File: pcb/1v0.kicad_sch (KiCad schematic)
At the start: 10 parts, among them U2 TPSM82903

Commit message: changes to power tree
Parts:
- added 1V0: TestPoint, TestPoint:TestPoint_Pad_D1.0mm, symbol library:TestPoint
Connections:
- net 1V0_FD: now also 1V0.1
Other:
- moved on the sheet: C3, C4, C7, FB1, R15, R16, R17, R6, R7, U2

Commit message: moved stuff around, bom
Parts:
- removed C7: 0.1uF, Capacitor_SMD:C_0402_1005Metric, symbol library:C
- removed R15, R17: 100, Resistor_SMD:R_0402_1005Metric, symbol library:R_US
- added C4: 4.7nF, Capacitor_SMD:C_0402_1005Metric, symbol library:C
- added C6: 0.1uF, Capacitor_SMD:C_0402_1005Metric, symbol library:C
- added R10, R12: 100, Resistor_SMD:R_0402_1005Metric, symbol library:R_US
- C3: footprint (none) -> library:C_0402_1005Metric; Manufacturer (none) -> Murata Electronics; Manufacturer Product Number (none) -> GRM155R61A106ME11D
- C5: renamed from C4; footprint (none) -> library:C_0402_1005Metric; Manufacturer (none) -> Murata Electronics; Manufacturer Product Number (none) -> GRM155R71C224KA12D
- R11: renamed from R16; footprint Resistor_SMD:R_0603_1608Metric -> Resistor_SMD:R_1206_3216Metric; Manufacturer (none) -> Vishay Dale; Manufacturer Product Number (none) -> WSLP12065L000FEA
- R8: renamed from R6; value R_US -> 10K 1%; footprint (none) -> library:R_0402_1005Metric; Manufacturer (none) -> Vishay Dale; Manufacturer Product Number (none) -> CRCW040210K0FKED
- R9: renamed from R7; value R_US -> 15K 1%; footprint (none) -> library:R_0402_1005Metric; Manufacturer (none) -> Vishay Dale; Manufacturer Product Number (none) -> CRCW040215K0FKED
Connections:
- net 1V0_FD: now also R12.2
- net 1V0_P: now also R10.2
- net 1V0_SENS_N: now also C6.1, R10.1
- net 1V0_SENS_P: now also C6.2, R12.1
- net GND: now also C4.2
- net at U2.5 (SS/TR): now also C4.1
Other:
- moved on the sheet: C3

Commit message: decoupling
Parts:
- R10, R12: value 100 -> 10; Manufacturer Product Number RC0402FR-07100RL -> RC0402FR-0710RL
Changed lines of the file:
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@@
-	(symbol
-		(lib_id "library:R_US")
-		(at 180.34 87.63 180)
-		(unit 1)
-		(exclude_from_sim no)
-		(in_bom yes)
-		(on_board yes)
-		(dnp no)
-		(property "Reference" "R12"
-			(at 182.88 86.36 0)
-			(effects
-				(font
-					(size 1.27 1.27)
-				)
-				(justify right)
-			)
-		)
-		(property "Value" "100"
-			(at 182.88 88.9 0)
-			(effects
-				(font
-					(size 1.27 1.27)
-				)
-				(justify right)
-			)
-		)
-		(property "Footprint" "Resistor_SMD:R_0402_1005Metric"
-			(at 179.324 87.376 90)
-			(effects
-				(font
-					(size 1.27 1.27)
-				)
-				(hide yes)
-			)
-		)
-		(property "Datasheet" "~"
-			(at 180.34 87.63 0)
-			(effects
-				(font
-					(size 1.27 1.27)
-				)
-				(hide yes)
-			)
-		)
-		(property "Description" "RES 100 OHM 1% 1/16W 0402"
-			(at 180.34 87.63 0)
-			(effects
-				(font
-					(size 1.27 1.27)
-				)
-				(hide yes)
-			)
-		)
-		(property "Manufacturer" "YAGEO"
-			(at 180.34 87.63 0)
-			(effects
-				(font
-					(size 1.27 1.27)
-				)
-				(hide yes)
-			)
-		)
-		(property "Manufacturer Product Number" "RC0402FR-07100RL"
-			(at 180.34 87.63 0)
-			(effects
-				(font
-					(size 1.27 1.27)
-				)
-				(hide yes)
-			)
-		)
-		(pin "1"
-		)
-		(pin "2"
-		)
-		(instances
-			(project "RPi-HwAB-1"
-				(path "/e63e39d7-6ac0-4ffd-8aa3-1841a4541b55/f9ebb56c-78c7-42ac-bc19-ccbf788f5318/543b0287-b025-45f5-b3a0-69295c58de1f"
-					(reference "R12")
-					(unit 1)
-				)
-			)
-		)
-	)
 	(symbol
 		(lib_id "library:R_US")
@@
 	)
 	(symbol
-		(lib_id "library:R_US")
-		(at 167.64 87.63 180)
-		(unit 1)
-		(exclude_from_sim no)
-		(in_bom yes)
-		(on_board yes)
-		(dnp no)
-		(property "Reference" "R10"
-			(at 165.1 86.36 0)
-			(effects
-				(font
-					(size 1.27 1.27)
-				)
-				(justify left)
-			)
-		)
-		(property "Value" "100"
-			(at 165.1 88.9 0)
-			(effects
-				(font
-					(size 1.27 1.27)
-				)
-				(justify left)
-			)
-		)
-		(property "Footprint" "Resistor_SMD:R_0402_1005Metric"
-			(at 166.624 87.376 90)
-			(effects
-				(font
-					(size 1.27 1.27)
-				)
-				(hide yes)
-			)
-		)
-		(property "Datasheet" "~"
-			(at 167.64 87.63 0)
-			(effects
-				(font
-					(size 1.27 1.27)
-				)
-				(hide yes)
-			)
-		)
-		(property "Description" "RES 100 OHM 1% 1/16W 0402"
-			(at 167.64 87.63 0)
-			(effects
-				(font
-					(size 1.27 1.27)
-				)
-				(hide yes)
-			)
-		)
-		(property "Manufacturer" "YAGEO"
-			(at 167.64 87.63 0)
-			(effects
-				(font
-					(size 1.27 1.27)
-				)
-				(hide yes)
-			)
-		)
-		(property "Manufacturer Product Number" "RC0402FR-07100RL"
-			(at 167.64 87.63 0)
-			(effects
-				(font
-					(size 1.27 1.27)
-				)
-				(hide yes)
-			)
-		)
-		(pin "1"
-		)
-		(pin "2"
-		)
-		(instances
-			(project "RPi-HwAB-1"
-				(path "/e63e39d7-6ac0-4ffd-8aa3-1841a4541b55/f9ebb56c-78c7-42ac-bc19-ccbf788f5318/543b0287-b025-45f5-b3a0-69295c58de1f"
-					(reference "R10")
-					(unit 1)
-				)
-			)
-		)
-	)
-	(symbol
 		(lib_id "library:C")
 		(at 78.74 107.95 0)
@@
 	)
 	(symbol
+		(lib_id "library:R_US")
+		(at 167.64 87.63 180)
+		(unit 1)
+		(exclude_from_sim no)
+		(in_bom yes)
+		(on_board yes)
+		(dnp no)
+		(property "Reference" "R10"
+			(at 165.1 86.36 0)
+			(effects
+				(font
+					(size 1.27 1.27)
+				)
+				(justify left)
+			)
+		)
+		(property "Value" "10"
+			(at 165.1 88.9 0)
+			(effects
+				(font
+					(size 1.27 1.27)
+				)
+				(justify left)
+			)
+		)
+		(property "Footprint" "Resistor_SMD:R_0402_1005Metric"
+			(at 166.624 87.376 90)
+			(effects
+				(font
+					(size 1.27 1.27)
+				)
+				(hide yes)
+			)
+		)
+		(property "Datasheet" "~"
+			(at 167.64 87.63 0)
+			(effects
+				(font
+					(size 1.27 1.27)
+				)
+				(hide yes)
+			)
+		)
+		(property "Description" "RES 10 OHM 1% 1/16W 0402"
+			(at 167.64 87.63 0)
+			(effects
+				(font
+					(size 1.27 1.27)
+				)
+				(hide yes)
+			)
+		)
+		(property "Manufacturer" "YAGEO"
+			(at 167.64 87.63 0)
+			(effects
+				(font
+					(size 1.27 1.27)
+				)
+				(hide yes)
+			)
+		)
+		(property "Manufacturer Product Number" "RC0402FR-0710RL"
+			(at 167.64 87.63 0)
+			(effects
+				(font
+					(size 1.27 1.27)
+				)
+				(hide yes)
+			)
+		)
+		(property "Name" ""
+			(at 167.64 87.63 0)
+			(effects
+				(font
+					(size 1.27 1.27)
+				)
+				(hide yes)
+			)
+		)
+		(pin "1"
+		)
+		(pin "2"
+		)
+		(instances
+			(project "RPi-HwAB-1"
+				(path "/e63e39d7-6ac0-4ffd-8aa3-1841a4541b55/f9ebb56c-78c7-42ac-bc19-ccbf788f5318/543b0287-b025-45f5-b3a0-69295c58de1f"
+					(reference "R10")
+					(unit 1)
+				)
+			)
+		)
+	)
+	(symbol
 		(lib_id "library:GND")
 		(at 78.74 114.3 0)
@@
 					(unit 1)
 				)
+			)
+		)
+	)
+	(symbol
+		(lib_id "library:R_US")
+		(at 180.34 87.63 180)
+		(unit 1)
+		(exclude_from_sim no)
+		(in_bom yes)
+		(on_board yes)
+		(dnp no)
+		(property "Reference" "R12"
+			(at 182.88 86.36 0)
+			(effects
+				(font
+					(size 1.27 1.27)
+				)
+				(justify right)
+			)
+		)
+		(property "Value" "10"
+			(at 182.88 88.9 0)
+			(effects
+				(font
+					(size 1.27 1.27)
+				)
+				(justify right)
+			)
+		)
+		(property "Footprint" "Resistor_SMD:R_0402_1005Metric"
+			(at 179.324 87.376 90)
+			(effects
+				(font
+					(size 1.27 1.27)
+				)
+				(hide yes)
+			)
+		)
+		(property "Datasheet" "~"
+			(at 180.34 87.63 0)
+			(effects
+				(font
+					(size 1.27 1.27)
+				)
+				(hide yes)
+			)
+		)
+		(property "Description" "RES 10 OHM 1% 1/16W 0402"
+			(at 180.34 87.63 0)
+			(effects
+				(font
+					(size 1.27 1.27)
+				)
+				(hide yes)
+			)
+		)
+		(property "Manufacturer" "YAGEO"
+			(at 180.34 87.63 0)
+			(effects
+				(font
+					(size 1.27 1.27)
+				)
+				(hide yes)
+			)
+		)
+		(property "Manufacturer Product Number" "RC0402FR-0710RL"
+			(at 180.34 87.63 0)
+			(effects
+				(font
+					(size 1.27 1.27)
+				)
+				(hide yes)
+			)
+		)
+		(property "Name" ""
+			(at 180.34 87.63 0)
+			(effects
+				(font
+					(size 1.27 1.27)
+				)
+				(hide yes)
+			)
+		)
+		(pin "1"
+		)
+		(pin "2"
+		)
+		(instances
+			(project "RPi-HwAB-1"
+				(path "/e63e39d7-6ac0-4ffd-8aa3-1841a4541b55/f9ebb56c-78c7-42ac-bc19-ccbf788f5318/543b0287-b025-45f5-b3a0-69295c58de1f"
+					(reference "R12")
+					(unit 1)
+				)

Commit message: bom
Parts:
- 1V0: now left out of the parts list
- C3: footprint library:C_0402_1005Metric -> Capacitor_SMD:C_0402_1005Metric; Part Description (none) -> CAP CER 10UF 10V X5R 0402
- C4: Part Description (none) -> CAP CER 0402 4.7NF 50V X7R 5%
- C5: footprint library:C_0402_1005Metric -> Capacitor_SMD:C_0603_1608Metric; Manufacturer Product Number GRM155R71C224KA12D -> GRM188R61A226ME15D; Part Description (none) -> CAP CER 22UF 10V X5R 0603
- C6: Part Description (none) -> CAP CER 0.1UF 16V X7R 0402
- FB1: value FerriteBead -> 120R @ 100MHz; footprint (none) -> Inductor_SMD:L_0603_1608Metric; Manufacturer (none) -> Murata Electronics; Manufacturer Product Number (none) -> BLM18KG121TN1D; Part Description (none) -> FERRITE BEAD 120 OHM 0603 1LN
- R10: renamed from R9; footprint library:R_0402_1005Metric -> Resistor_SMD:R_0402_1005Metric; Part Description (none) -> RES 15K OHM 1% 1/16W 0402
- R11: renamed from R10; Part Description (none) -> RES 10 OHM 1% 1/16W 0402
- R12: renamed from R11; Part Description (none) -> RES 0.005 OHM 1% 1W 1206
- R13: renamed from R12; Part Description (none) -> RES 10 OHM 1% 1/16W 0402
- R9: renamed from R8; footprint library:R_0402_1005Metric -> Resistor_SMD:R_0402_1005Metric; Part Description (none) -> RES 10K OHM 1% 1/16W 0402
- U2: Part Description (none) -> 3-V TO 17-V, 3-A, HIGH-EFFICIENC
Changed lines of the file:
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@@
 		(on_board yes)
 		(dnp no)
-		(property "Reference" "R11"
+		(property "Reference" "R12"
 			(at 173.99 77.47 90)
 			(effects
@@
 			)
 		)
+		(property "Part Description" "RES 0.005 OHM 1% 1W 1206"
+			(at 173.99 81.28 90)
+			(effects
+				(font
+					(size 1.27 1.27)
+				)
+				(hide yes)
+			)
+		)
 		(pin "1"
 		)
@@
 			(project "RPi-HwAB-1"
 				(path "/e63e39d7-6ac0-4ffd-8aa3-1841a4541b55/f9ebb56c-78c7-42ac-bc19-ccbf788f5318/543b0287-b025-45f5-b3a0-69295c58de1f"
-					(reference "R11")
+					(reference "R12")
 					(unit 1)
 				)
@@
 			)
 		)
-		(property "Datasheet" ""
+		(property "Datasheet" "~"
 			(at 78.74 107.95 0)
 			(effects
@@
 		)
 		(property "Name" ""
+			(at 78.74 107.95 0)
+			(effects
+				(font
+					(size 1.27 1.27)
+				)
+				(hide yes)
+			)
+		)
+		(property "Part Description" "CAP CER 0402 4.7NF 50V X7R 5%"
 			(at 78.74 107.95 0)
 			(effects
@@
 			)
 		)
-		(property "Value" "FerriteBead"
+		(property "Value" "120R @ 100MHz"
 			(at 210.7692 86.36 90)
 			(effects
@@
 			)
 		)
-		(property "Footprint" ""
+		(property "Footprint" "Inductor_SMD:L_0603_1608Metric"
 			(at 210.82 93.218 90)
 			(effects
@@
 		(property "Description" "Ferrite bead"
 			(at 210.82 91.44 0)
+			(effects
+				(font
+					(size 1.27 1.27)
+				)
+				(hide yes)
+			)
+		)
+		(property "Manufacturer" "Murata Electronics"
+			(at 210.82 91.44 90)
+			(effects
+				(font
+					(size 1.27 1.27)
+				)
+				(hide yes)
+			)
+		)
+		(property "Manufacturer Product Number" "BLM18KG121TN1D"
+			(at 210.82 91.44 90)
+			(effects
+				(font
+					(size 1.27 1.27)
+				)
+				(hide yes)
+			)
+		)
+		(property "Name" ""
+			(at 210.82 91.44 0)
+			(effects
+				(font
+					(size 1.27 1.27)
+				)
+				(hide yes)
+			)
+		)
+		(property "Part Description" "FERRITE BEAD 120 OHM 0603 1LN"
+			(at 210.82 91.44 90)
 			(effects
 				(font
@@
 			)
 		)
+		(property "Part Description" "3-V TO 17-V, 3-A, HIGH-EFFICIENC"
+			(at 106.68 96.52 0)
+			(effects
+				(font
+					(size 1.27 1.27)
+				)
+				(hide yes)
+			)
+		)
 		(pin "11"
 		)
@@
 		(on_board yes)
 		(dnp no)
-		(property "Reference" "R10"
+		(property "Reference" "R11"
 			(at 165.1 86.36 0)
 			(effects
@@
 			)
 		)
+		(property "Part Description" "RES 10 OHM 1% 1/16W 0402"
+			(at 167.64 87.63 0)
+			(effects
+				(font
+					(size 1.27 1.27)
+				)
+				(hide yes)
+			)
+		)
 		(pin "1"
 		)
@@
 			(project "RPi-HwAB-1"
 				(path "/e63e39d7-6ac0-4ffd-8aa3-1841a4541b55/f9ebb56c-78c7-42ac-bc19-ccbf788f5318/543b0287-b025-45f5-b3a0-69295c58de1f"
-					(reference "R10")
+					(reference "R11")
 					(unit 1)
 				)
@@
 		(unit 1)
 		(exclude_from_sim no)
-		(in_bom yes)
+		(in_bom no)
 		(on_board yes)
 		(dnp no)
@@
 			)
 		)
+		(property "Name" ""
+			(at 231.14 66.04 0)
+			(effects
+				(font
+					(size 1.27 1.27)
+				)
+				(hide yes)
+			)
+		)
 		(pin "1"
 		)
@@
 		(dnp no)
 		(fields_autoplaced yes)
-		(property "Reference" "R9"
+		(property "Reference" "R10"
 			(at 137.16 99.0599 0)
 			(effects
@@
 			)
 		)
-		(property "Footprint" "library:R_0402_1005Metric"
+		(property "Footprint" "Resistor_SMD:R_0402_1005Metric"
 			(at 135.636 100.584 90)
 			(effects
@@
 			)
 		)
+		(property "Part Description" "RES 15K OHM 1% 1/16W 0402"
+			(at 134.62 100.33 0)
+			(effects
+				(font
+					(size 1.27 1.27)
+				)
+				(hide yes)
+			)
+		)
 		(pin "1"
 		)
@@
 			(project "RPi-HwAB-1"
 				(path "/e63e39d7-6ac0-4ffd-8aa3-1841a4541b55/f9ebb56c-78c7-42ac-bc19-ccbf788f5318/543b0287-b025-45f5-b3a0-69295c58de1f"
-					(reference "R9")
+					(reference "R10")
 					(unit 1)
 				)
@@
 		(on_board yes)
 		(dnp no)
-		(property "Reference" "R12"
+		(property "Reference" "R13"
 			(at 182.88 86.36 0)
 			(effects
@@
 			)
 		)
+		(property "Part Description" "RES 10 OHM 1% 1/16W 0402"
+			(at 180.34 87.63 0)
+			(effects
+				(font
+					(size 1.27 1.27)
+				)
+				(hide yes)
+			)
+		)
 		(pin "1"
 		)
@@
 			(project "RPi-HwAB-1"
 				(path "/e63e39d7-6ac0-4ffd-8aa3-1841a4541b55/f9ebb56c-78c7-42ac-bc19-ccbf788f5318/543b0287-b025-45f5-b3a0-69295c58de1f"
-					(reference "R12")
+					(reference "R13")
 					(unit 1)
 				)
@@
 		(dnp no)
 		(fields_autoplaced yes)
-		(property "Reference" "R8"
+		(property "Reference" "R9"
 			(at 137.16 86.3599 0)
 			(effects
@@
 			)
 		)
-		(property "Footprint" "library:R_0402_1005Metric"
+		(property "Footprint" "Resistor_SMD:R_0402_1005Metric"
 			(at 135.636 87.884 90)
 			(effects
@@
 			)
 		)
+		(property "Part Description" "RES 10K OHM 1% 1/16W 0402"
+			(at 134.62 87.63 0)
+			(effects
+				(font
+					(size 1.27 1.27)
+				)
+				(hide yes)
+			)
+		)
 		(pin "1"
 		)
@@
 			(project "RPi-HwAB-1"
 				(path "/e63e39d7-6ac0-4ffd-8aa3-1841a4541b55/f9ebb56c-78c7-42ac-bc19-ccbf788f5318/543b0287-b025-45f5-b3a0-69295c58de1f"
-					(reference "R8")
+					(reference "R9")
 					(unit 1)
 				)
@@
 			)
 		)
-		(property "Footprint" "library:C_0402_1005Metric"
+		(property "Footprint" "Capacitor_SMD:C_0402_1005Metric"
 			(at 72.0852 111.76 0)
 			(effects
@@
 		)
 		(property "Manufacturer Product Number" "GRM155R61A106ME11D"
+			(at 71.12 107.95 0)
+			(effects
+				(font
+					(size 1.27 1.27)
+				)
+				(hide yes)
+			)
+		)
+		(property "Part Description" "CAP CER 10UF 10V X5R 0402"
 			(at 71.12 107.95 0)
 			(effects
@@
 			)
 		)
+		(property "Part Description" "CAP CER 0.1UF 16V X7R 0402"
+			(at 173.99 96.52 90)
+			(effects
+				(font
+					(size 1.27 1.27)
+				)
+				(hide yes)
+			)
+		)
 		(pin "1"
 		)
@@
 			)
 		)
-		(property "Footprint" "library:C_0402_1005Metric"
+		(property "Footprint" "Capacitor_SMD:C_0603_1608Metric"
 			(at 146.3548 97.79 0)
 			(effects
@@
 			)
 		)
-		(property "Manufacturer Product Number" "GRM155R71C224KA12D"
+		(property "Manufacturer Product Number" "GRM188R61A226ME15D"
 			(at 147.32 93.98 0)
 			(effects
+				(font
+					(size 1.27 1.27)
+				)
+				(hide yes)
+			)
+		)
+		(property "Part Description" "CAP CER 22UF 10V X5R 0603"
+			(at 147.32 93.98 0)
+			(effects

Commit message: added mig ddr pinout constraints
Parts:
- C5: renamed from C3; footprint Capacitor_SMD:C_0402_1005Metric -> Capacitor_SMD:C_1206_3216Metric; Manufacturer Murata Electronics -> KYOCERA AVX; Manufacturer Product Number GRM155R61A106ME11D -> TAJA106M010RNJ; Part Description CAP CER 10UF 10V X5R 0402 -> CAP TANT 10UF 20% 10V 1206
- renumbered C5 to C3, C6 to C4, C4 to C6, R9 to R10, R13 to R12, R10 to R13, R12 to R9
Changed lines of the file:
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@@
 		(on_board yes)
 		(dnp no)
-		(property "Reference" "R12"
+		(property "Reference" "R9"
 			(at 173.99 77.47 90)
 			(effects
@@
 			(project "RPi-HwAB-1"
 				(path "/e63e39d7-6ac0-4ffd-8aa3-1841a4541b55/f9ebb56c-78c7-42ac-bc19-ccbf788f5318/543b0287-b025-45f5-b3a0-69295c58de1f"
-					(reference "R12")
+					(reference "R9")
 					(unit 1)
 				)
@@
 		(on_board yes)
 		(dnp no)
-		(property "Reference" "C4"
+		(property "Reference" "C6"
 			(at 82.55 106.68 0)
 			(effects
@@
 			(project "RPi-HwAB-1"
 				(path "/e63e39d7-6ac0-4ffd-8aa3-1841a4541b55/f9ebb56c-78c7-42ac-bc19-ccbf788f5318/543b0287-b025-45f5-b3a0-69295c58de1f"
-					(reference "C4")
+					(reference "C6")
 					(unit 1)
 				)
@@
 		(dnp no)
 		(fields_autoplaced yes)
-		(property "Reference" "R10"
+		(property "Reference" "R13"
 			(at 137.16 99.0599 0)
 			(effects
@@
 			(project "RPi-HwAB-1"
 				(path "/e63e39d7-6ac0-4ffd-8aa3-1841a4541b55/f9ebb56c-78c7-42ac-bc19-ccbf788f5318/543b0287-b025-45f5-b3a0-69295c58de1f"
-					(reference "R10")
+					(reference "R13")
 					(unit 1)
 				)
@@
 		(on_board yes)
 		(dnp no)
-		(property "Reference" "R13"
+		(property "Reference" "R12"
 			(at 182.88 86.36 0)
 			(effects
@@
 			(project "RPi-HwAB-1"
 				(path "/e63e39d7-6ac0-4ffd-8aa3-1841a4541b55/f9ebb56c-78c7-42ac-bc19-ccbf788f5318/543b0287-b025-45f5-b3a0-69295c58de1f"
-					(reference "R13")
+					(reference "R12")
 					(unit 1)
 				)
@@
 		(dnp no)
 		(fields_autoplaced yes)
-		(property "Reference" "R9"
+		(property "Reference" "R10"
 			(at 137.16 86.3599 0)
 			(effects
@@
 			(project "RPi-HwAB-1"
 				(path "/e63e39d7-6ac0-4ffd-8aa3-1841a4541b55/f9ebb56c-78c7-42ac-bc19-ccbf788f5318/543b0287-b025-45f5-b3a0-69295c58de1f"
-					(reference "R9")
+					(reference "R10")
 					(unit 1)
 				)
@@
 		(on_board yes)
 		(dnp no)
-		(property "Reference" "C3"
+		(property "Reference" "C5"
 			(at 67.31 106.6799 0)
 			(effects
@@
 			)
 		)
-		(property "Footprint" "Capacitor_SMD:C_0402_1005Metric"
+		(property "Footprint" "Capacitor_SMD:C_1206_3216Metric"
 			(at 72.0852 111.76 0)
 			(effects
@@
 			)
 		)
-		(property "Manufacturer" "Murata Electronics"
+		(property "Manufacturer" "KYOCERA AVX"
 			(at 71.12 107.95 0)
 			(effects
@@
 			)
 		)
-		(property "Manufacturer Product Number" "GRM155R61A106ME11D"
+		(property "Manufacturer Product Number" "TAJA106M010RNJ"
 			(at 71.12 107.95 0)
 			(effects
@@
 			)
 		)
-		(property "Part Description" "CAP CER 10UF 10V X5R 0402"
+		(property "Part Description" "CAP TANT 10UF 20% 10V 1206"
 			(at 71.12 107.95 0)
 			(effects
@@
 			(project "RPi-HwAB-1"
 				(path "/e63e39d7-6ac0-4ffd-8aa3-1841a4541b55/f9ebb56c-78c7-42ac-bc19-ccbf788f5318/543b0287-b025-45f5-b3a0-69295c58de1f"
-					(reference "C3")
+					(reference "C5")
 					(unit 1)
 				)
@@
 		(dnp no)
 		(fields_autoplaced yes)
-		(property "Reference" "C6"
+		(property "Reference" "C4"
 			(at 173.99 88.9 90)
 			(effects
@@
 			(project "RPi-HwAB-1"
 				(path "/e63e39d7-6ac0-4ffd-8aa3-1841a4541b55/f9ebb56c-78c7-42ac-bc19-ccbf788f5318/543b0287-b025-45f5-b3a0-69295c58de1f"
-					(reference "C6")
+					(reference "C4")
 					(unit 1)
 				)
@@
 		(on_board yes)
 		(dnp no)
-		(property "Reference" "C5"
+		(property "Reference" "C3"
 			(at 151.13 92.7099 0)
 			(effects
@@
 			(project "RPi-HwAB-1"
 				(path "/e63e39d7-6ac0-4ffd-8aa3-1841a4541b55/f9ebb56c-78c7-42ac-bc19-ccbf788f5318/543b0287-b025-45f5-b3a0-69295c58de1f"
-					(reference "C5")
-					(unit 1)
-				)
+					(reference "C3")
+					(unit 1)
+				)

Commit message: restructured power, power plane layout
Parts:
- removed 1V0: TestPoint, TestPoint:TestPoint_Pad_D1.0mm, symbol library:TestPoint
- added R11: 20K, Resistor_SMD:R_0402_1005Metric, symbol library:R_US
- renumbered R13 to R10, R9 to R6, R10 to R7, R11 to R8, R12 to R9
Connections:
- net 1V0_PG: now also R11.1
- net 5V0: now also R11.2
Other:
- moved on the sheet: C3, C4, C5, C6, FB1, R10, R6, R7, R8, R9, U2

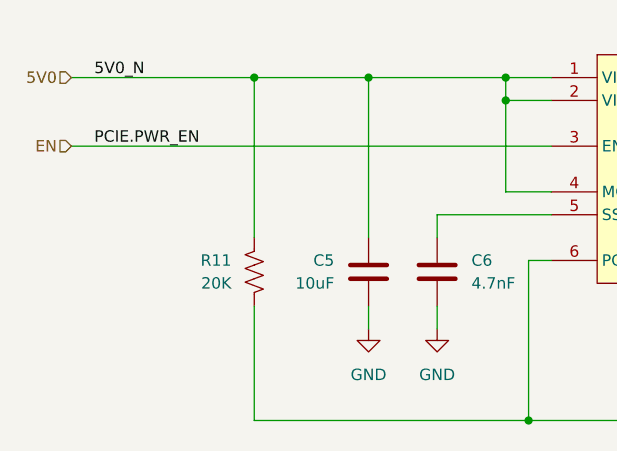
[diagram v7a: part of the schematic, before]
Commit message: added jlc fab
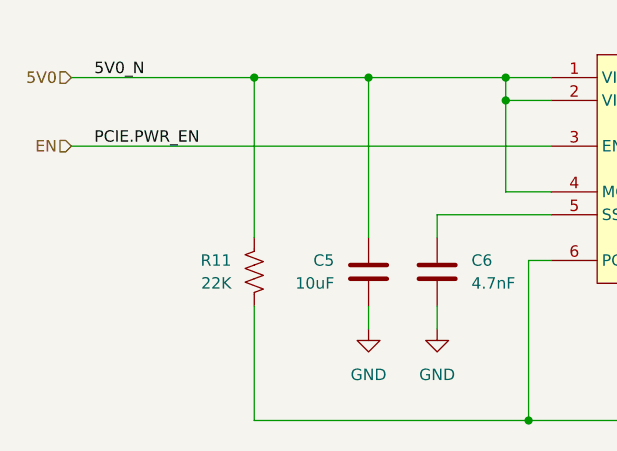
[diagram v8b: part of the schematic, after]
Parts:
- R11: value 20K -> 22K
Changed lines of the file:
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@@
 			)
 		)
-		(property "Value" "20K"
+		(property "Value" "22K"
 			(at 63.5 109.2199 0)
 			(show_name no)
